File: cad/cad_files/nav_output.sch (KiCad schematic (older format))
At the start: 8 parts

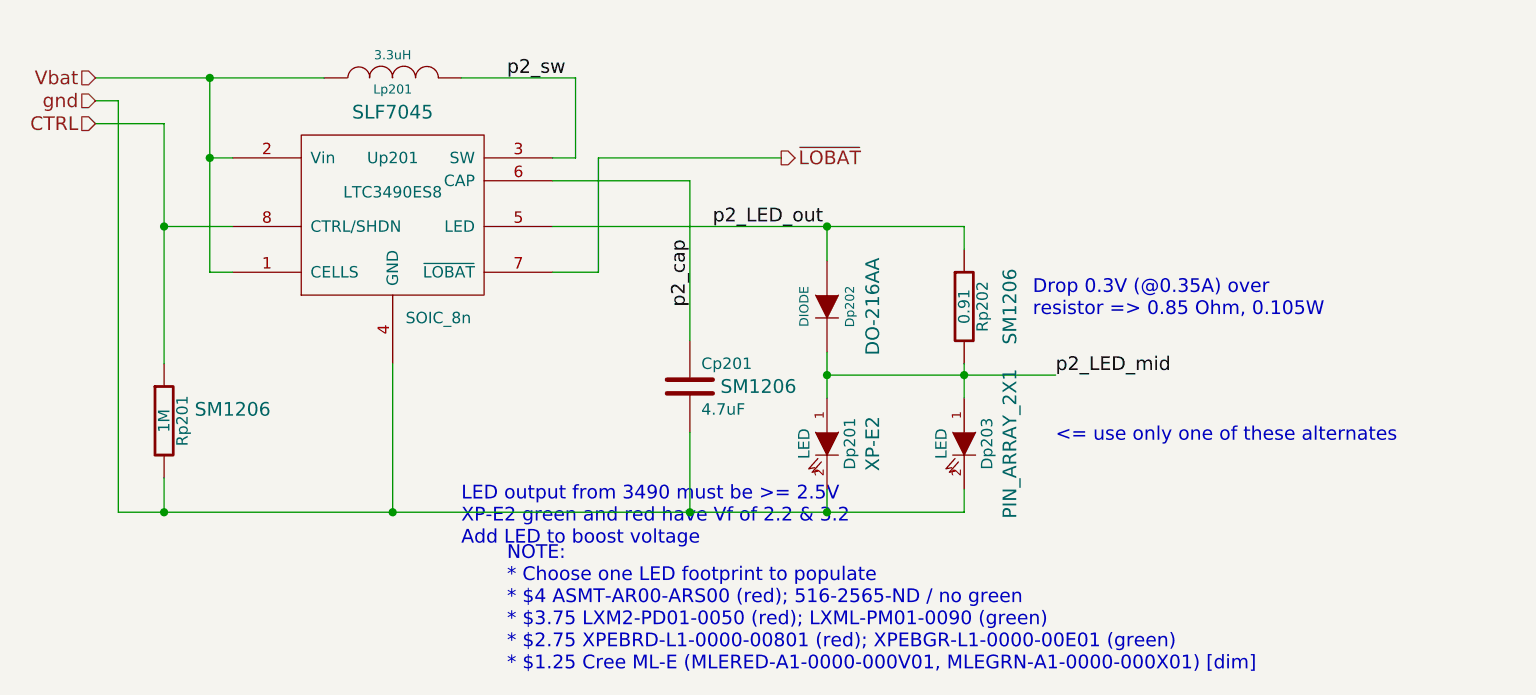
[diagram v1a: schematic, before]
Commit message: Bom updating (and schematic) for LED power
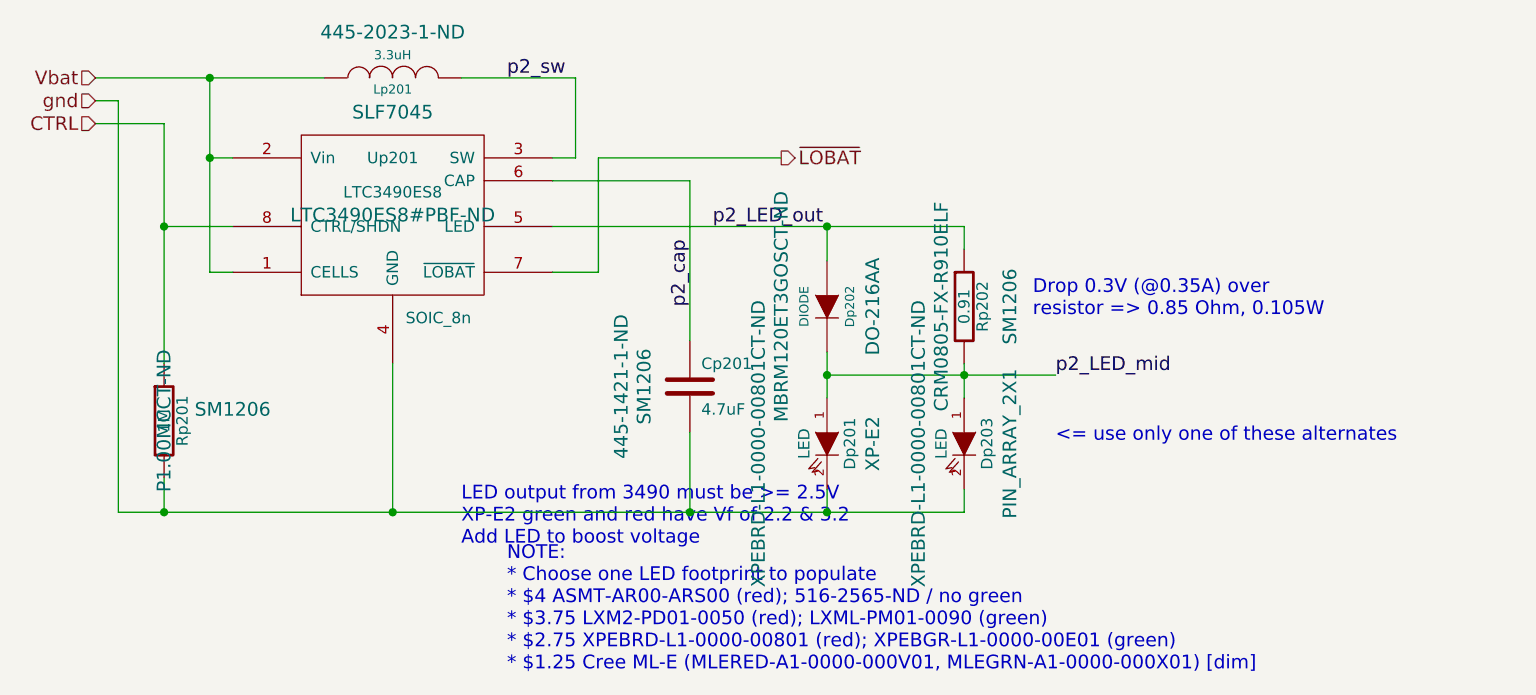
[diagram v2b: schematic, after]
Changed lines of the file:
@@
-EESchema Schematic File Version 2  date Wed 24 Dec 2014 07:01:58 AM HST
+EESchema Schematic File Version 2  date Wed 24 Dec 2014 07:52:56 AM HST
 LIBS:local_parts
 LIBS:power
@@
 F 1 "LED" H 7500 4900 50  0000 C CNN
 F 2 "PIN_ARRAY_2X1" H 7500 5200 60  0000 C CNN
-F 4 "XPEBRD-L1-0000-00801CT-ND" H 7500 5000 60  0001 C CNN "digikey"
+F 4 "XPEBRD-L1-0000-00801CT-ND" H 7500 4800 60  0000 C CNN "digikey"
 	1    7500 5000
 	0    1    1    0
@@
 F 1 "0.91" V 7500 4400 50  0000 C CNN
 F 2 "SM1206" V 7700 4400 60  0000 C CNN
-F 4 "CRM0805-FX-R910ELF" V 7500 4400 60  0001 C CNN "digikey"
+F 4 "CRM0805-FX-R910ELF" V 7400 4400 60  0000 C CNN "digikey"
 	1    7500 4400
 	1    0    0    -1
@@
 F 1 "DIODE" H 6900 4300 40  0000 C CNN
 F 2 "DO-216AA" H 6900 4600 60  0000 C CNN
-F 4 "MBRM120ET3GOSCT-ND" H 6900 4400 60  0001 C CNN "digikey"
+F 4 "MBRM120ET3GOSCT-ND" H 6900 4200 60  0000 C CNN "digikey"
 	1    6900 4400
 	0    1    1    0
@@
 F 1 "LED" H 6900 4900 50  0000 C CNN
 F 2 "XP-E2" H 6900 5200 60  0000 C CNN
-F 4 "XPEBRD-L1-0000-00801CT-ND" H 6900 5000 60  0001 C CNN "digikey"
+F 4 "XPEBRD-L1-0000-00801CT-ND" H 6900 4700 60  0000 C CNN "digikey"
 	1    6900 5000
 	0    1    1    0
@@
 F 1 "3.3uH" V 5100 3400 40  0000 C CNN
 F 2 "SLF7045" V 4850 3400 60  0000 C CNN
-F 4 "445-2023-1-ND" V 5000 3400 60  0001 C CNN "digikey"
+F 4 "445-2023-1-ND" V 5200 3400 60  0000 C CNN "digikey"
 	1    5000 3400
 	0    -1   -1   0
@@
 F 0 "Cp201" H 6350 4850 50  0000 L CNN
 F 1 "4.7uF" H 6350 4650 50  0000 L CNN
-F 2 "SM1206" H 6600 4750 60  0000 C CNN
-F 4 "445-1421-1-ND" H 6300 4750 60  0001 C CNN "digikey"
+F 2 "SM1206" V 6100 4750 60  0000 C CNN
+F 4 "445-1421-1-ND" V 6000 4750 60  0000 C CNN "digikey"
 	1    6300 4750
 	1    0    0    -1
@@
 F 1 "1M" V 4000 4900 50  0000 C CNN
 F 2 "SM1206" H 4300 4950 60  0000 C CNN
-F 4 "P1.00MCCT-ND" V 4000 4900 60  0001 C CNN "digikey"
+F 4 "P1.00MCCT-ND" V 4000 4900 60  0000 C CNN "digikey"
 	1    4000 4900
 	1    0    0    -1
@@
 F 2 "SOIC_8n" H 5200 3550 50  0000 C CNN
 F 3 "DOCUMENTATION" H 5000 4000 50  0001 C CNN
-F 4 "LTC3490ES8#PBF-ND" H 5000 4000 60  0001 C CNN "digikey"
+F 4 "LTC3490ES8#PBF-ND" H 5000 4000 60  0000 C CNN "digikey"
 	1    5000 4000
 	1    0    0    -1
